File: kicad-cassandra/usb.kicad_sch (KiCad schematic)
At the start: 9 parts, among them J2 USB_C_Receptacle_USB2.0_16P, U1 MIC69153YME-TR

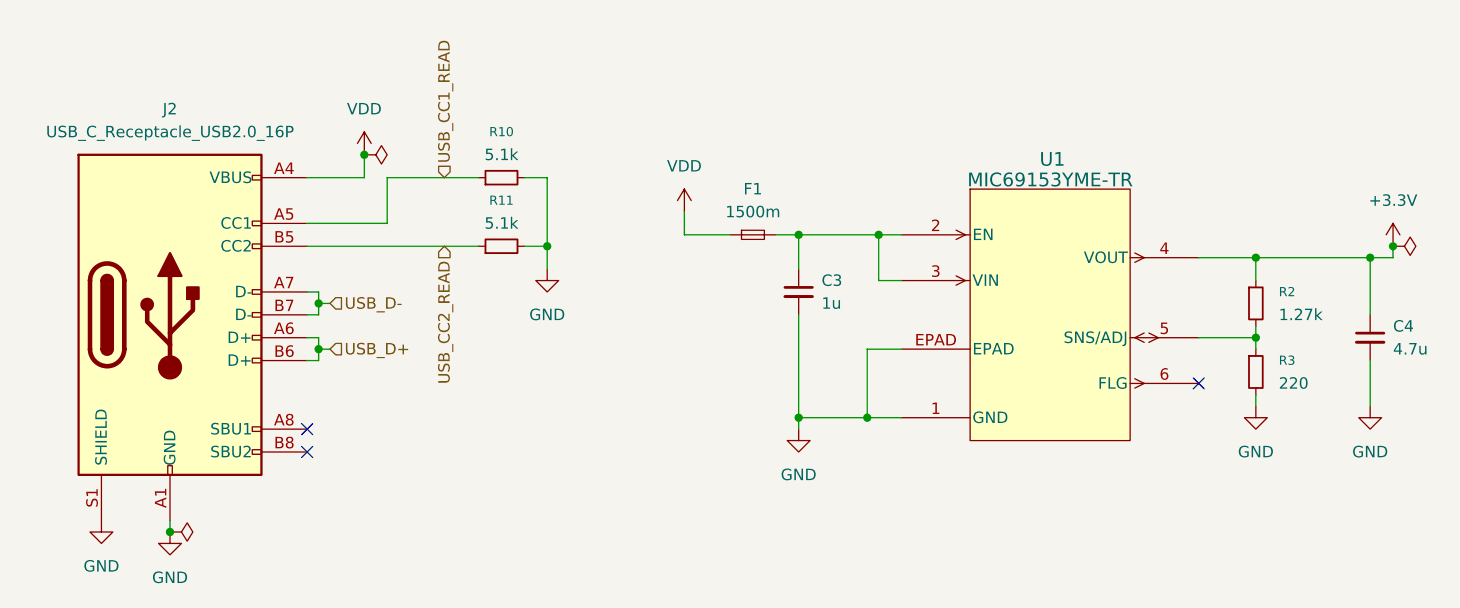
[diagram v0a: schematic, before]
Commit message: use rohm ldo
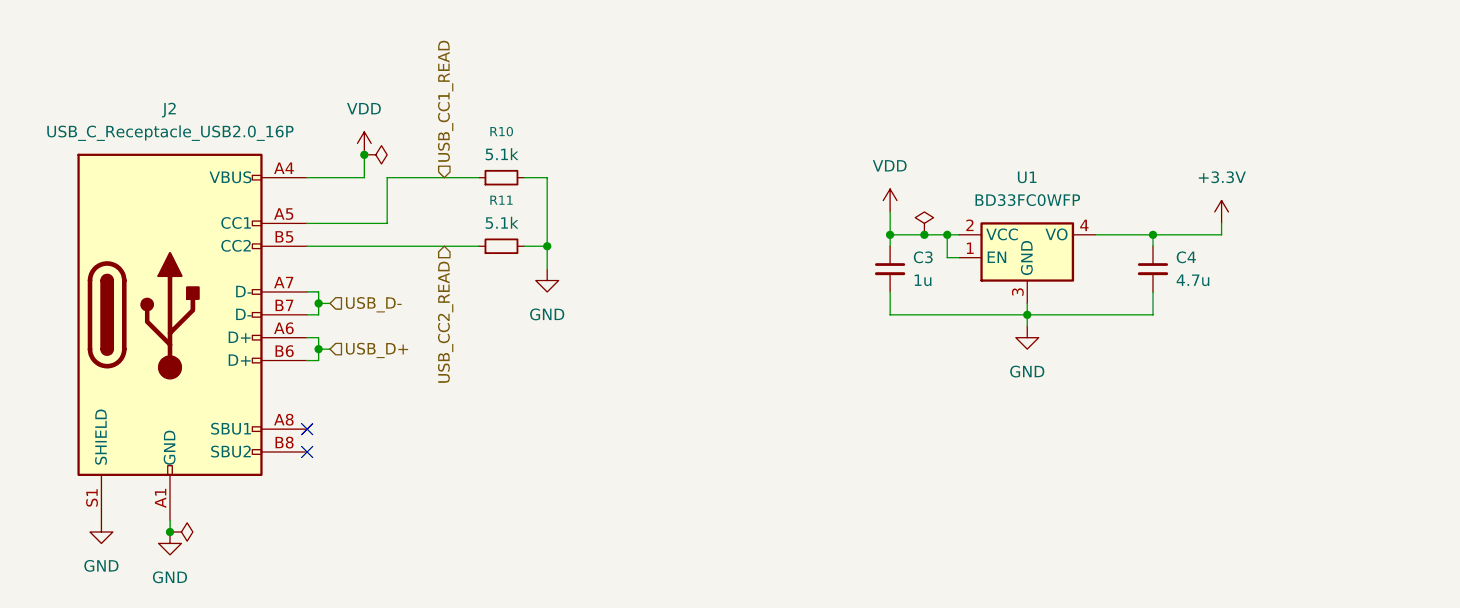
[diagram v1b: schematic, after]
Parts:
- removed F1: 1500m, Fuse:Fuse_0603_1608Metric_Pad1.05x0.95mm_HandSolder, symbol Device:Fuse_Small
- removed R2: 1.27k, Resistor_SMD:R_0603_1608Metric_Pad0.98x0.95mm_HandSolder, symbol Device:R_Small
- removed R3: 220, Resistor_SMD:R_0603_1608Metric_Pad0.98x0.95mm_HandSolder, symbol Device:R_Small
- removed U1: MIC69153YME-TR, cassandra:SOIC-8_ME_MCH-L, symbol cassandra:MIC69153YME-TR
- added U1: BD33FC0WFP, Package_TO_SOT_SMD:TO-252-4, symbol Regulator_Linear:BD33FC0WFP
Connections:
- net +3.3V: now also U1.4 (VO)
- net GND: now also U1.3 (GND)
- net VDD: now also C3.1, U1.1 (EN), U1.2 (VCC)
- no-connect marks 3 -> 2
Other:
- moved on the sheet: C3, C4

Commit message: add wire only possibility
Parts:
- added J8: ~, cassandra:CONN4_05010302_WRE, symbol cassandra:691401700002B
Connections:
- net GND: now also J8.1, J8.A1 (1)
- net VDD: now also J8.2, J8.A2 (2)
- net USB_CC1_READ: no longer names the net of J2.A5 (CC1), R10.1
- net USB_CC2_READ: no longer names the net of J2.B5 (CC2), R11.1
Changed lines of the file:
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@@
 	(title_block
 		(title "cassandra")
-		(date "2025-11-22")
-		(rev "rev0")
+		(date "2026-04-16")
+		(rev "rev3")
 		(company "by ayham")
 		(comment 1 "sapientia")
@@
 	)
 	(junction
+		(at 175.26 78.74)
+		(diameter 0)
+		(color 0 0 0 0)
+	)
+	(junction
 		(at 137.16 81.28)
 		(diameter 0)
@@
 	(wire
 		(pts
+			(xy 165.1 78.74) (xy 175.26 78.74)
+		)
+		(stroke
+			(width 0)
+			(type default)
+		)
+	)
+	(wire
+		(pts
 			(xy 119.38 73.66) (xy 129.54 73.66)
 		)
@@
 	(wire
 		(pts
-			(xy 175.26 77.47) (xy 175.26 80.01)
+			(xy 175.26 77.47) (xy 175.26 78.74)
 		)
 		(stroke
@@
 	(wire
 		(pts
+			(xy 156.21 78.74) (xy 156.21 82.55)
+		)
+		(stroke
+			(width 0)
+			(type default)
+		)
+	)
+	(wire
+		(pts
 			(xy 110.49 88.9) (xy 111.76 88.9)
 		)
@@
 	(wire
 		(pts
+			(xy 175.26 78.74) (xy 175.26 80.01)
+		)
+		(stroke
+			(width 0)
+			(type default)
+		)
+	)
+	(wire
+		(pts
 			(xy 110.49 81.28) (xy 129.54 81.28)
+		)
+		(stroke
+			(width 0)
+			(type default)
+		)
+	)
+	(wire
+		(pts
+			(xy 162.56 78.74) (xy 156.21 78.74)
 		)
 		(stroke
@@
 		)
 	)
-	(hierarchical_label "USB_CC2_READ"
-		(shape input)
-		(at 125.73 81.28 270)
-		(effects
-			(font
-				(size 1.27 1.27)
-			)
-			(justify right)
-		)
-	)
 	(hierarchical_label "USB_D+"
 		(shape input)
 		(at 113.03 92.71 0)
-		(effects
-			(font
-				(size 1.27 1.27)
-			)
-			(justify left)
-		)
-	)
-	(hierarchical_label "USB_CC1_READ"
-		(shape input)
-		(at 125.73 73.66 90)
 		(effects
 			(font
@@
 	)
 	(symbol
+		(lib_id "power:GND")
+		(at 156.21 82.55 0)
+		(unit 1)
+		(exclude_from_sim no)
+		(in_bom yes)
+		(on_board yes)
+		(dnp no)
+		(fields_autoplaced yes)
+		(property "Reference" "#PWR011"
+			(at 156.21 88.9 0)
+			(effects
+				(font
+					(size 1.27 1.27)
+				)
+				(hide yes)
+			)
+		)
+		(property "Value" "GND"
+			(at 156.21 87.63 0)
+			(effects
+				(font
+					(size 1.27 1.27)
+				)
+			)
+		)
+		(property "Footprint" ""
+			(at 156.21 82.55 0)
+			(effects
+				(font
+					(size 1.27 1.27)
+				)
+				(hide yes)
+			)
+		)
+		(property "Datasheet" ""
+			(at 156.21 82.55 0)
+			(effects
+				(font
+					(size 1.27 1.27)
+				)
+				(hide yes)
+			)
+		)
+		(property "Description" "Power symbol creates a global label with name \"GND\" , ground"
+			(at 156.21 82.55 0)
+			(effects
+				(font
+					(size 1.27 1.27)
+				)
+				(hide yes)
+			)
+		)
+		(pin "1"
+		)
+		(instances
+			(project "kicad-cassandra"
+				(path "/dc25841e-5b7b-45f5-9f4d-5995b2d288b6/9d8f6675-6f97-45cd-aead-a18f3375a83a"
+					(reference "#PWR011")
+					(unit 1)
+				)
+			)
+		)
+	)
+	(symbol
 		(lib_id "power:PWR_FLAG")
 		(at 95.25 113.03 270)
@@
 					(unit 1)
 				)
+			)
+		)
+	)
+	(symbol
+		(lib_id "cassandra:691401700002B")
+		(at 165.1 83.82 0)
+		(mirror x)
+		(unit 1)
+		(exclude_from_sim no)
+		(in_bom yes)
+		(on_board yes)
+		(dnp no)
+		(property "Reference" "J8"
+			(at 160.02 81.28 0)
+			(effects
+				(font
+					(size 1.016 0.8636)
+				)
+				(justify right)
+			)
+		)
+		(property "Value" "~"
+			(at 160.02 83.82 0)
+			(effects
+				(font
+					(size 1.016 0.8636)
+				)
+				(justify right)
+			)
+		)
+		(property "Footprint" "cassandra:CONN4_05010302_WRE"
+			(at 165.1 83.82 0)
+			(effects
+				(font
+					(size 1.27 1.27)
+				)
+				(hide yes)
+			)
+		)
+		(property "Datasheet" ""
+			(at 165.1 83.82 0)
+			(effects
+				(font
+					(size 1.27 1.27)
+				)
+				(hide yes)
+			)
+		)
+		(property "Description" "WR-TBL Serie 401B - 5.00 mm Screwless Vertical Entry - 2.0 mm 2 Wires\n\nKIND PROPERTIES\n\nPitch 5 mm\n\nMATERIAL PROPERTIES\n\nInsulator Material PA66\nInsulator Flammability Rating UL94 V-0\nContact Material Brass\nContact Plating Tin\nWire Guard Material Stainless Steel\n\nGENERAL INFORMATION\n\nOperating Temperature -40 up to +105 °C\nCompliance RoHS\n\nELECTRICAL PROPERTIES\n\nIR cULus 10 A\nIR VDE 16 A\nWorking Voltage [cULus] 300 V (AC)\nWorking Voltage [VDE] 450 V (AC)\nWithstanding Voltage [cULus] 2000 V (AC)\nContact Resistance [cULus] 20 mΩ\nContact Resistance [VDE] 20 mΩ\n\nMechanical Properties\n\nWire Strip Length 9 up to 10 (mm)\n\nWire Properties\n\nSolid Wire Section (AWG) 14 to 24 (AWG)\nSolid Wire Section (Metric) 2.08 to 0.205 (mm²)\nStranded Wire Section (AWG) 14 to 24 (AWG)\nStranded Wire Section (Metric) 2.08 to 0.205 (mm²)\n\nCERTIFICATION\n\ncULus Approval E315414\nVDE Approval 40036896\n\nPackaging Properties\n\nPackaging Box\n\nhttps://www.we-online.com/catalog/media/o33321v209%20Family_WR-TBL_6914017000xxB.jpg\n\nDetails see: https://www.we-online.com/catalog/en/TBL_5_00_401B_SCREWLESS_VERTICAL_ENTRY_2_0MM2_WIRES_6914017000XXB/ https://www.we-online.com/catalog/en/TBL_5_00_401B_SCREWLESS_VERTICAL_ENTRY_2_0MM2_WIRES_6914017000XXB/\n\nUpdated by Ella Wu  2019-12-31\n2019(C) Wurth Elektronik"
+			(at 165.1 83.82 0)
+			(effects
+				(font
+					(size 1.27 1.27)
+				)
+				(hide yes)
+			)
+		)
+		(pin "A2"
+		)
+		(pin "2"
+		)
+		(pin "A1"
+		)
+		(pin "1"
+		)
+		(instances
+			(project "kicad-cassandra"
+				(path "/dc25841e-5b7b-45f5-9f4d-5995b2d288b6/9d8f6675-6f97-45cd-aead-a18f3375a83a"
+					(reference "J8")
+					(unit 1)
+				)
